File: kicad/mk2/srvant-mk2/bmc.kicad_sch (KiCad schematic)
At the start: 38 parts, among them J3 Conn_01x03, J4 USB_OTG, J6 Conn_02x05_Odd_Even, SW1 POWER, SW2 EMMC_KEY, SW3 RST, SW4 HOST_RESET, U22 TMP1075DSG, U25 74AHC1G08, U5 rp-t113-s3, U6 PCF85063AT/AAZ, U7 TPD4EUSB30, U8 74LVC2G07, Y1 X32K768S301

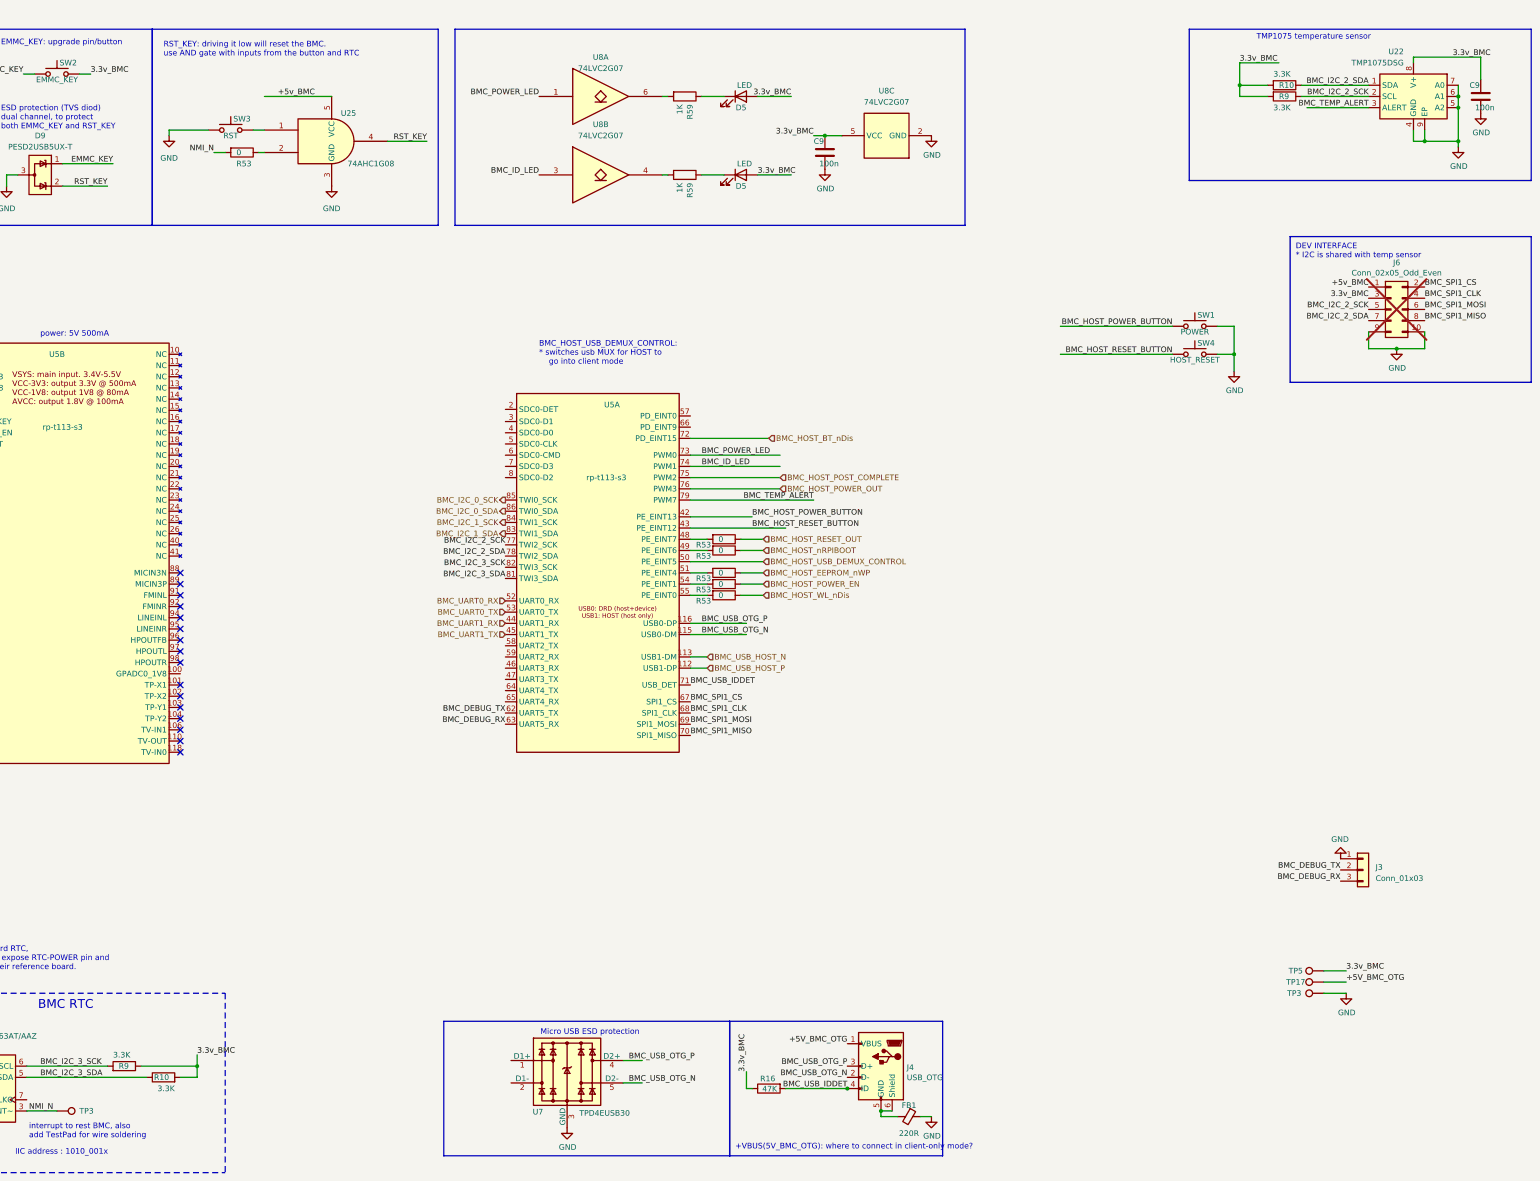
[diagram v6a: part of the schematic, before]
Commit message: add rp-t113-s3 datasheets (cn), make CI happier
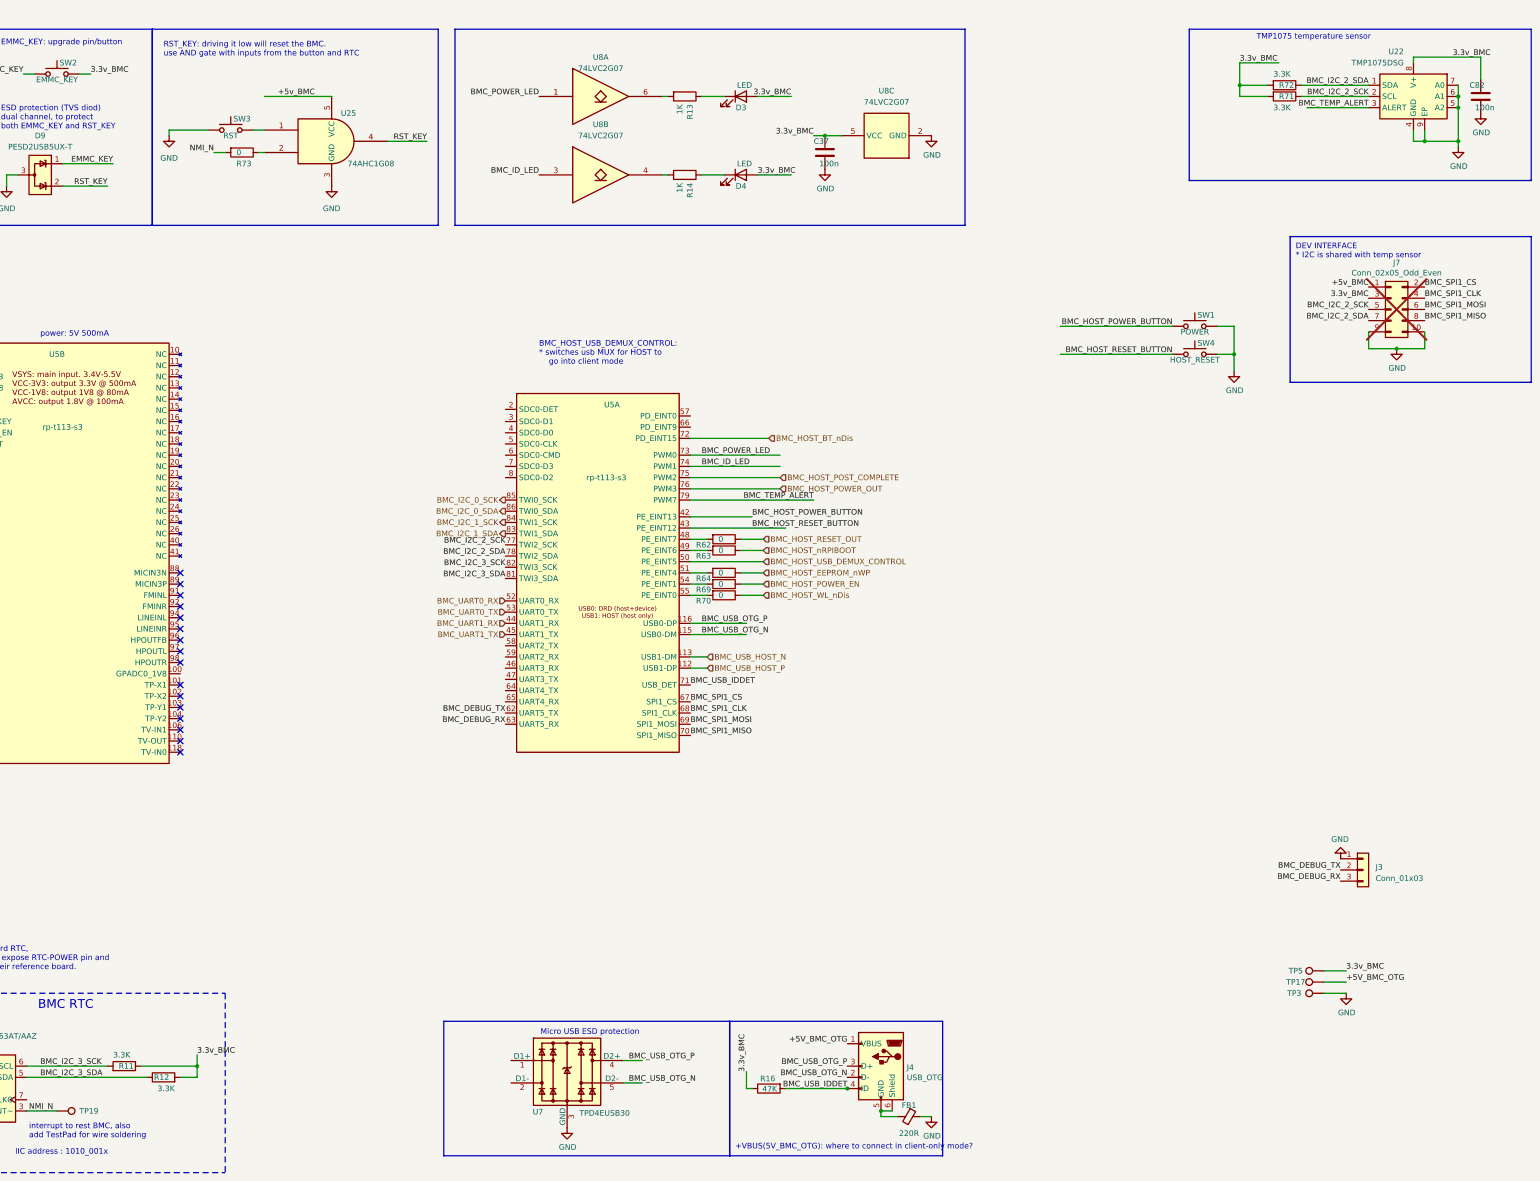
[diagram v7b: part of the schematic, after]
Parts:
- C37, C82: renamed from C9; mouser# 963-EMK105B7104KV-F -> 963-EMK105B7104KV-F
- D3, D4: renamed from D5; Field4 Digikey -> Digikey; Field5 LTST-S270KRKT -> LTST-S270KRKT
- FB1: manf# BLM15PX221SH1D -> BLM15PX221SH1D; mouser# 81-BLM15PX221SH1D -> 81-BLM15PX221SH1D
- U8: manf# SN74LVC2G07DBVR -> SN74LVC2G07DBVR; mouser# 595-SN74LVC2G07DBVR -> 595-SN74LVC2G07DBVR
- renumbered J6 to J7, R9 to R11, R10 to R12, R59 to R13, R59 to R14, R53 to R62, R53 to R63, R53 to R64, R53 to R69, R53 to R70, R9 to R71, R10 to R72, R53 to R73, TP3 to TP19

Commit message: fix 3d models. again
Once again assign all the 3d models to the components.
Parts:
- U5: footprint rp-t113-s3:rp-t113-s3 -> footprints:rp-t113-s3
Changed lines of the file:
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@@
       (effects (font (size 1.27 1.27)))
     )
-    (property "Footprint" "rp-t113-s3:rp-t113-s3" (at 171.45 119.38 0)
+    (property "Footprint" "footprints:rp-t113-s3" (at 171.45 119.38 0)
       (effects (font (size 1.27 1.27)) hide)
     )
@@
       (effects (font (size 1.27 1.27)))
     )
-    (property "Footprint" "rp-t113-s3:rp-t113-s3" (at 46.99 106.68 0)
-      (effects (font (size 1.27 1.27)) hide)
-    )
+    (property "Footprint" "footprints:rp-t113-s3" (at 46.99 106.68 0)
+      (effects (font (size 1.27 1.27)) hide)
+    )
